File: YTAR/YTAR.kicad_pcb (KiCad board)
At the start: 6 copper layers, 50 x 50 mm, 231 parts, among them J1 STDC14, J2 CAMERA, J3 Micro_Sd, J4 FH12-40S-0.5SH(55), J5 USB_C_USB4085-GF-A, J6 IO, SW1 RESET, SW2 PICTURE, SW3 MODE, U1 STM32H750XBHx, U2 MCP2562-E-MF, U3 DS90C124, U5 TPS56339, U6 TPS56339, Y1 25MHz

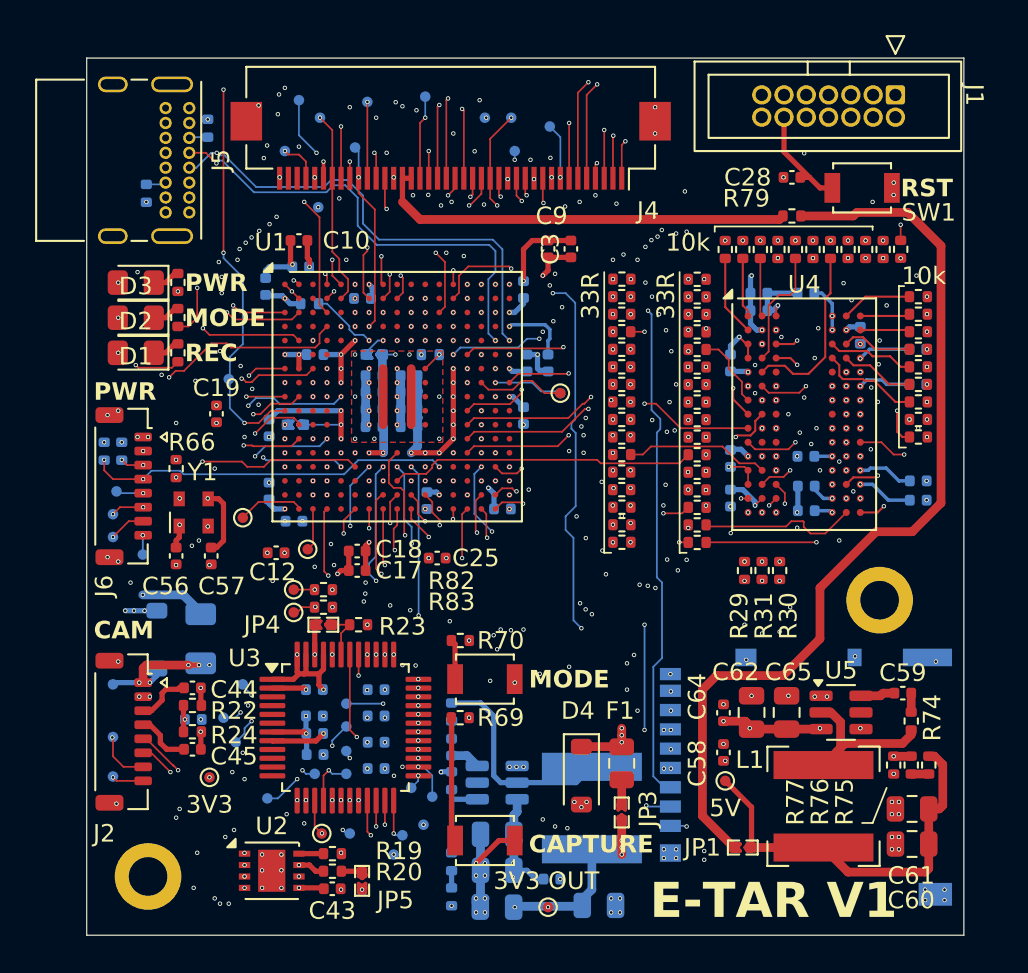
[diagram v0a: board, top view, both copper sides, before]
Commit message: Dodano TP. Jest ladniej
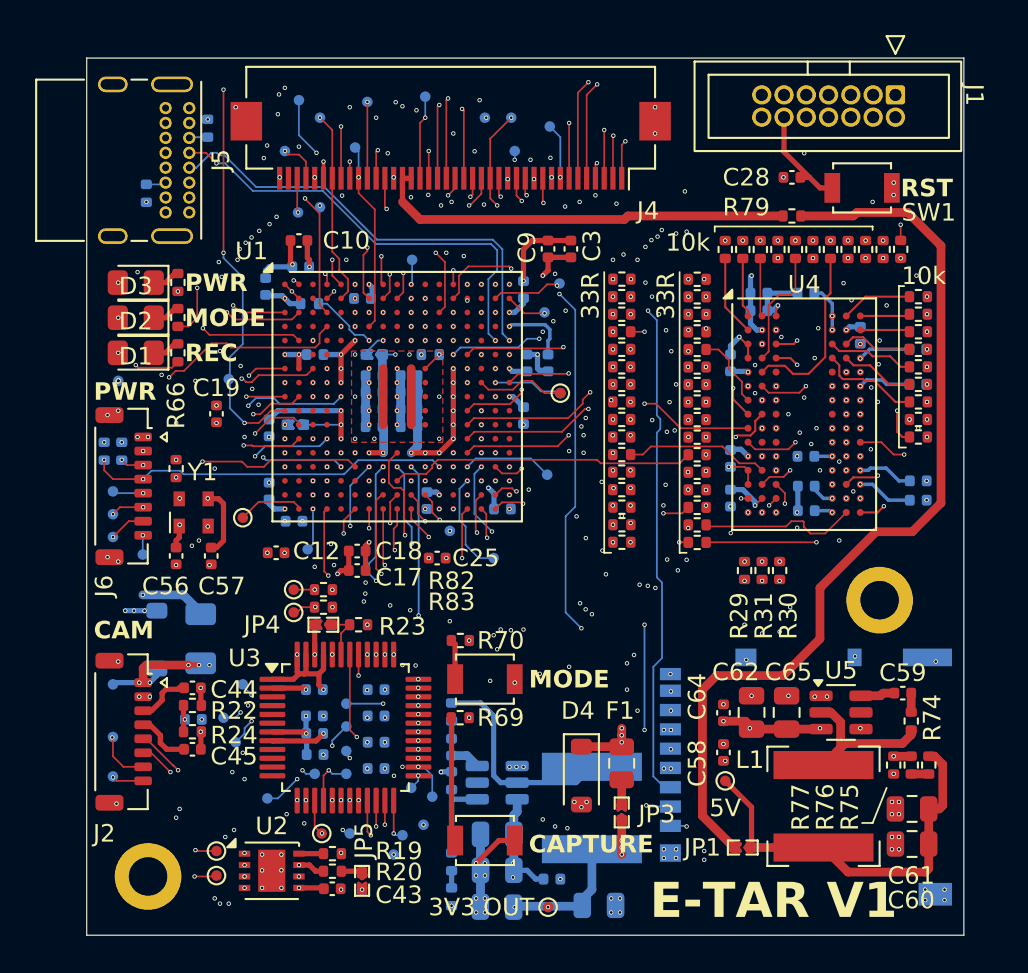
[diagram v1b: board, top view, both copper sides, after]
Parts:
- added TP45: ~, MEMS_Custom:TestPoint_Pad_D0.6mm_SMT, B.Cu at (30.6, 23.5)
- added TP46: ~, MEMS_Custom:TestPoint_Pad_D0.6mm_SMT, B.Cu at (24.1, 20.8)
- added TP47: D1, MEMS_Custom:TestPoint_Pad_D0.6mm_SMT, B.Cu at (32.7, 39.0)
- added TP48: D2, MEMS_Custom:TestPoint_Pad_D0.6mm_SMT, B.Cu at (38.2, 35.8)
- added TP49: D3, MEMS_Custom:TestPoint_Pad_D0.6mm_SMT, B.Cu at (35.2, 40.5)
- added TP50: D4, MEMS_Custom:TestPoint_Pad_D0.6mm_SMT, B.Cu at (38.1, 26.5)
- added TP51: D11, MEMS_Custom:TestPoint_Pad_D0.6mm_SMT, B.Cu at (39.0, 24.9)
- added TP52: RX, MEMS_Custom:TestPoint_Pad_D0.6mm_SMT, F.Cu at (19.4, 58.6)
- added TP53: TX, MEMS_Custom:TestPoint_Pad_D0.6mm_SMT, F.Cu at (19.4, 57.2)
- added TP54: GND, MEMS_Custom:TestPoint_Pad_D0.6mm_SMT, B.Cu at (13.8, 30.4)
- TP13, TP41: moved to B.Cu
- moved TP13 24.8 mm to (13.8, 28.8), turned to 180 degrees
- moved TP34 0.20 mm to (13.5, 36.7)
- moved TP6 0.10 mm to (25.3, 20.5)
- turned TP41 to 180 degrees
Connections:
- U1 pad A10: unconnected-(U1-PG9-PadA10) -> /DCMI_VSYNC
- U1 pad A3: /DCMI_VSYNC -> unconnected-(U1-PI5-PadA3)
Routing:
- net /DCMI_D3: track 0.00 -> 5.89 mm, vias 0 -> 1
- net /DCMI_D2: track 0.00 -> 5.13 mm, vias 0 -> 1
- net /DCMI_D1: track 0.00 -> 3.90 mm, vias 0 -> 2
- net /DCMI_D11: track 0.00 -> 3.87 mm, vias 0 -> 1
- net Net-(U1-PE0): track 45.9 -> 42.5 mm
- net /DCMI_D4: track 0.00 -> 2.35 mm, vias 0 -> 1
- net /LCD_AUX_4: track 0.00 -> 1.97 mm, vias 0 -> 1
- net /DCMI_VSYNC: track 0.00 -> 1.42 mm, vias 0 -> 1
- net /D-: track 28.8 -> 27.5 mm, vias 2 -> 1
- net /D+: track 28.5 -> 27.3 mm
- net /FD_CAN1_TX: track 41.5 -> 42.6 mm
- net /LCD_HSYNC: track 22.2 -> 23.2 mm
- net Net-(U1-PH7): track 10.4 -> 9.48 mm
- net /FD_CAN1_RX: track 44.4 -> 45.3 mm
- net /SD_CK: track 40.0 -> 39.4 mm
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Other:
- board text added: "K. SURMA M. ZYCHLA Ł. ŚWISZCZ"

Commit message: Almost ready to fly
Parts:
- removed JP6: VDDA, MEMS_Custom:JP_0402_OPEN
- added R84: 0R, Resistor_SMD:R_0402_1005Metric, B.Cu at (23.9, 32.8)
- moved TP16 1.01 mm to (20.6, 46.8)
- moved TP47 0.57 mm to (32.5, 39.5)
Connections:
- J4 pad 39: /LCD_AUX_5 -> GND
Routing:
- net GND: track 64.0 -> 66.8 mm, vias 190 -> 184
- net /ROUT0: track 28.8 -> 29.9 mm
- net Net-(U1-PF5): track 47.1 -> 46.3 mm
- net Net-(U1-PF1): track 41.1 -> 41.8 mm
- net Net-(U1-PF4): track 47.9 -> 47.3 mm
- net /I2C2_SCL: track 17.8 -> 18.1 mm, vias 3 -> 2
- net +3.3V: track 84.1 -> 83.8 mm, vias 82 -> 81
- net /LCD_B3: track 8.58 -> 8.66 mm, vias 3 -> 2
- net +12V_CAM: track 79.4 -> 79.5 mm, vias 15 -> 14
- net Net-(C69-Pad1): vias 6 -> 5
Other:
- board text added: "K. SURMA M. ZYCHLA Ł. ŚWISZCZ 2024"
- board text removed: "K. SURMA M. ZYCHLA Ł. ŚWISZCZ"

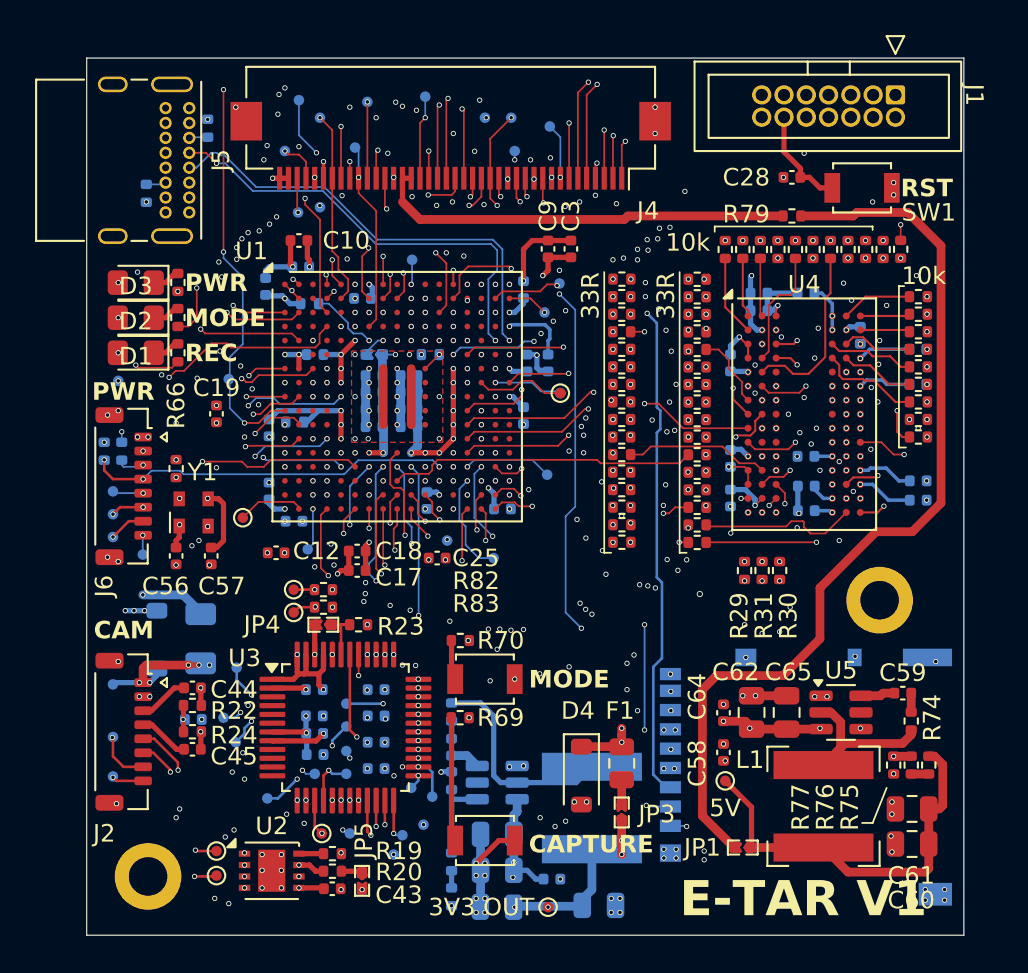
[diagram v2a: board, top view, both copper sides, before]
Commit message: USB matched
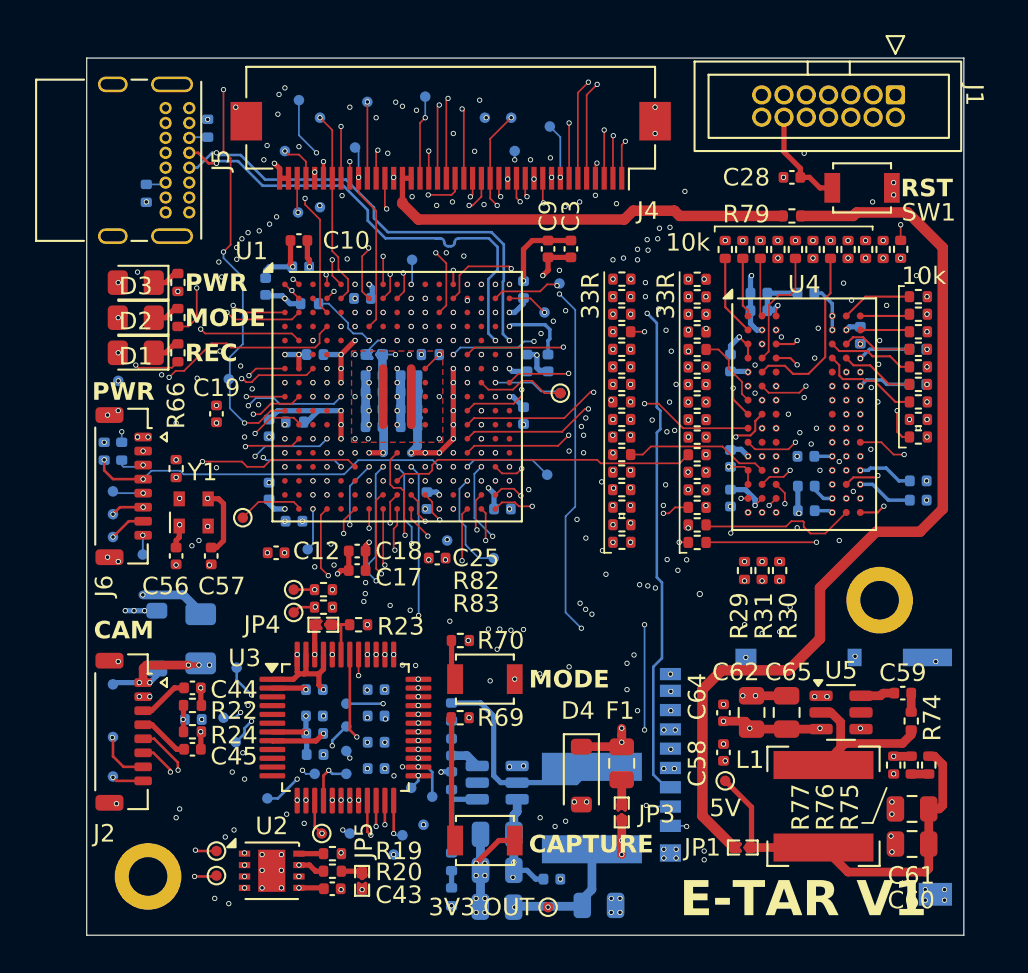
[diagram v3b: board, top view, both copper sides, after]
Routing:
- net /D+: track 27.3 -> 28.1 mm
- net /D-: track 27.5 -> 28.1 mm, vias 1 -> 2
- net GND: track 66.8 -> 67.3 mm
